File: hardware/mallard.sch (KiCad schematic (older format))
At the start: 84 parts, among them J1 USB_A, J2 Conn_02x03_Odd_Even, J3 Conn_01x03, J4 Conn_01x03, J5 Conn_01x03, J6 Conn_01x03, SW1 RESET Switch, U1 TMP235, U10 LM828, U11 STM32L4Q5xx, U12 LTC3529EDCB, U2 TMP235, U3 TMP235, U4 BQ24210DQCT, U5 TMUX1309, U6 TMUX1309, U7 LMP7721, U8 TPS71710DRVR, U9 LMV554

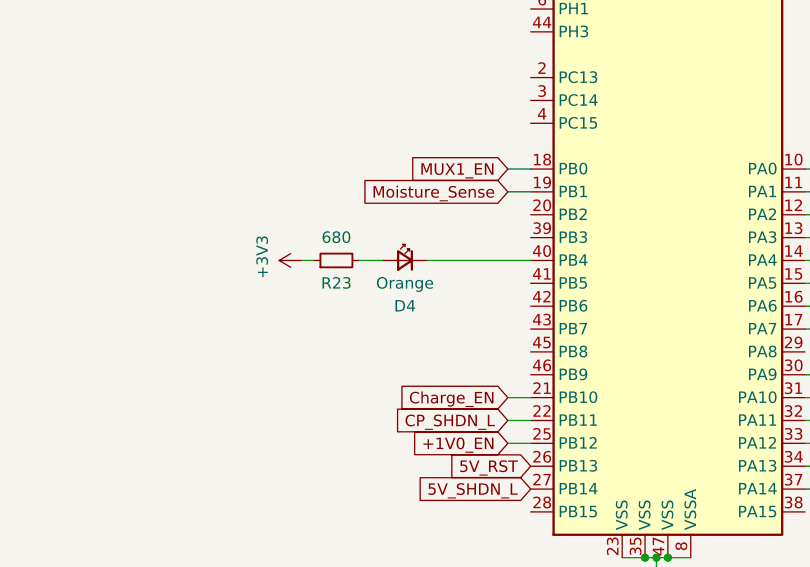
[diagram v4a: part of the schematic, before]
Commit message: Found alts for passives
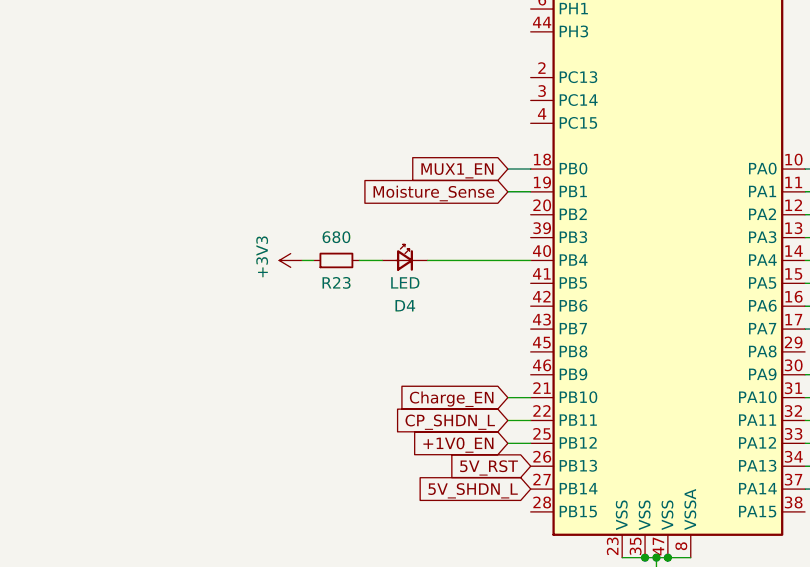
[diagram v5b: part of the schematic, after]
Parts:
- C1, C10, C12, C13, C14, C15, C2, C21, C3, C4, C5, C6, C7, C8, C9: Digikey 311-1446-1-ND -> CL10B105KO8NNNC
- D1: Digikey S1B-FDICT-ND -> S1BFSCT-ND
- D4: value Orange -> LED; footprint Diode_SMD:D_0805_2012Metric_Castellated -> LED_SMD:LED_0603_1608Metric_Pad1.05x0.95mm_HandSolder; Digikey 160-1413-1-ND -> 1497-1215-1-ND
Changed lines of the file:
@@
 AR Path="/61F56C19" Ref="D4"  Part="1"
 F 0 "D4" H 15900 6050 50  0000 C CNN
-F 1 "Orange" H 15900 6150 50  0000 C CNN
-F 2 "Diode_SMD:D_0805_2012Metric_Castellated" V 15900 6250 50  0001 C CNN
-F 3 "https://optoelectronics.liteon.com/upload/download/DS-22-99-0185/LTST-C170KFKT.pdf" V 15900 6250 50  0001 C CNN
-F 4 "160-1413-1-ND" H 15900 6250 50  0001 C CNN "Digikey"
+F 1 "LED" H 15900 6150 50  0000 C CNN
+F 2 "LED_SMD:LED_0603_1608Metric_Pad1.05x0.95mm_HandSolder" V 15900 6250 50  0001 C CNN
+F 3 "https://www.sunledusa.com/products/spec/XZVG53W-8.pdf" V 15900 6250 50  0001 C CNN
+F 4 "1497-1215-1-ND" H 15900 6250 50  0001 C CNN "Digikey"
 	1    15900 6250
 	-1   0    0    -1
@@
 F 1 "1uF" H -3535 12705 50  0000 L CNN
 F 2 "Capacitor_SMD:C_0603_1608Metric_Pad1.08x0.95mm_HandSolder" H -3612 12600 50  0001 C CNN
-F 3 "https://www.yageo.com/upload/media/product/productsearch/datasheet/mlcc/UPY-GPHC_X7R_6.3V-to-50V_20.pdf" H -3650 12750 50  0001 C CNN
-F 4 "311-1446-1-ND" H -3650 12750 50  0001 C CNN "Digikey"
+F 3 "http://weblib.samsungsem.com/mlcc/mlcc-ec-data-sheet.do?partNumber=CL10B105KO8NNN" H -3650 12750 50  0001 C CNN
+F 4 "CL10B105KO8NNNC" H -3650 12750 50  0001 C CNN "Digikey"
 	1    -3650 12750
 	1    0    0    -1
@@
 F 1 "1uF" H -2585 9455 50  0000 L CNN
 F 2 "Capacitor_SMD:C_0603_1608Metric_Pad1.08x0.95mm_HandSolder" H -2662 9350 50  0001 C CNN
-F 3 "https://www.yageo.com/upload/media/product/productsearch/datasheet/mlcc/UPY-GPHC_X7R_6.3V-to-50V_20.pdf" H -2700 9500 50  0001 C CNN
-F 4 "311-1446-1-ND" H -2700 9500 50  0001 C CNN "Digikey"
+F 3 "http://weblib.samsungsem.com/mlcc/mlcc-ec-data-sheet.do?partNumber=CL10B105KO8NNN" H -2700 9500 50  0001 C CNN
+F 4 "CL10B105KO8NNNC" H -2700 9500 50  0001 C CNN "Digikey"
 	1    -2700 9500
 	1    0    0    -1
@@
 F 1 "1uF" H -2385 11855 50  0000 L CNN
 F 2 "Capacitor_SMD:C_0603_1608Metric_Pad1.08x0.95mm_HandSolder" H -2462 11750 50  0001 C CNN
-F 3 "https://www.yageo.com/upload/media/product/productsearch/datasheet/mlcc/UPY-GPHC_X7R_6.3V-to-50V_20.pdf" H -2500 11900 50  0001 C CNN
-F 4 "311-1446-1-ND" H -2500 11900 50  0001 C CNN "Digikey"
+F 3 "http://weblib.samsungsem.com/mlcc/mlcc-ec-data-sheet.do?partNumber=CL10B105KO8NNN" H -2500 11900 50  0001 C CNN
+F 4 "CL10B105KO8NNNC" H -2500 11900 50  0001 C CNN "Digikey"
 	1    -2500 11900
 	1    0    0    -1
@@
 F 1 "1uF" H 2265 10055 50  0000 L CNN
 F 2 "Capacitor_SMD:C_0603_1608Metric_Pad1.08x0.95mm_HandSolder" H 2188 9950 50  0001 C CNN
-F 3 "https://www.yageo.com/upload/media/product/productsearch/datasheet/mlcc/UPY-GPHC_X7R_6.3V-to-50V_20.pdf" H 2150 10100 50  0001 C CNN
-F 4 "311-1446-1-ND" H 2150 10100 50  0001 C CNN "Digikey"
+F 3 "http://weblib.samsungsem.com/mlcc/mlcc-ec-data-sheet.do?partNumber=CL10B105KO8NNN" H 2150 10100 50  0001 C CNN
+F 4 "CL10B105KO8NNNC" H 2150 10100 50  0001 C CNN "Digikey"
 	1    2150 10100
 	1    0    0    -1
@@
 F 1 "1uF" H 1815 11055 50  0000 L CNN
 F 2 "Capacitor_SMD:C_0603_1608Metric_Pad1.08x0.95mm_HandSolder" H 1738 10950 50  0001 C CNN
-F 3 "https://www.yageo.com/upload/media/product/productsearch/datasheet/mlcc/UPY-GPHC_X7R_6.3V-to-50V_20.pdf" H 1700 11100 50  0001 C CNN
-F 4 "311-1446-1-ND" H 1700 11100 50  0001 C CNN "Digikey"
+F 3 "http://weblib.samsungsem.com/mlcc/mlcc-ec-data-sheet.do?partNumber=CL10B105KO8NNN" H 1700 11100 50  0001 C CNN
+F 4 "CL10B105KO8NNNC" H 1700 11100 50  0001 C CNN "Digikey"
 	1    1700 11100
 	1    0    0    -1
@@
 F 1 "1uF" H 6315 3255 50  0000 L CNN
 F 2 "Capacitor_SMD:C_0603_1608Metric_Pad1.08x0.95mm_HandSolder" H 6238 3150 50  0001 C CNN
-F 3 "https://www.yageo.com/upload/media/product/productsearch/datasheet/mlcc/UPY-GPHC_X7R_6.3V-to-50V_20.pdf" H 6200 3300 50  0001 C CNN
-F 4 "311-1446-1-ND" H 6200 3300 50  0001 C CNN "Digikey"
+F 3 "http://weblib.samsungsem.com/mlcc/mlcc-ec-data-sheet.do?partNumber=CL10B105KO8NNN" H 6200 3300 50  0001 C CNN
+F 4 "CL10B105KO8NNNC" H 6200 3300 50  0001 C CNN "Digikey"
 	1    6200 3300
 	1    0    0    -1
@@
 F 2 "Diode_SMD:D_SMA_Handsoldering" H 1600 3000 50  0001 C CNN
 F 3 "https://www.diodes.com/assets/Datasheets/ds16003.pdf" H 1600 3000 50  0001 C CNN
-F 4 "S1B-FDICT-ND" H 1600 3000 50  0001 C CNN "Digikey"
+F 4 "S1BFSCT-ND" H 1600 3000 50  0001 C CNN "Digikey"
 	1    1600 3000
 	-1   0    0    1
@@
 F 1 "1uF" H 8065 4605 50  0000 L CNN
 F 2 "Capacitor_SMD:C_0603_1608Metric_Pad1.08x0.95mm_HandSolder" H 7988 4500 50  0001 C CNN
-F 3 "https://www.yageo.com/upload/media/product/productsearch/datasheet/mlcc/UPY-GPHC_X7R_6.3V-to-50V_20.pdf" H 7950 4650 50  0001 C CNN
-F 4 "311-1446-1-ND" H 7950 4650 50  0001 C CNN "Digikey"
+F 3 "http://weblib.samsungsem.com/mlcc/mlcc-ec-data-sheet.do?partNumber=CL10B105KO8NNN" H 7950 4650 50  0001 C CNN
+F 4 "CL10B105KO8NNNC" H 7950 4650 50  0001 C CNN "Digikey"
 	1    7950 4650
 	1    0    0    -1
@@
 F 1 "1uF" H 10265 4605 50  0000 L CNN
 F 2 "Capacitor_SMD:C_0603_1608Metric_Pad1.08x0.95mm_HandSolder" H 10188 4500 50  0001 C CNN
-F 3 "https://www.yageo.com/upload/media/product/productsearch/datasheet/mlcc/UPY-GPHC_X7R_6.3V-to-50V_20.pdf" H 10150 4650 50  0001 C CNN
-F 4 "311-1446-1-ND" H 10150 4650 50  0001 C CNN "Digikey"
+F 3 "http://weblib.samsungsem.com/mlcc/mlcc-ec-data-sheet.do?partNumber=CL10B105KO8NNN" H 10150 4650 50  0001 C CNN
+F 4 "CL10B105KO8NNNC" H 10150 4650 50  0001 C CNN "Digikey"
 	1    10150 4650
 	1    0    0    -1
@@
 F 1 "1uF" H 2265 3205 50  0000 L CNN
 F 2 "Capacitor_SMD:C_0603_1608Metric_Pad1.08x0.95mm_HandSolder" H 2188 3100 50  0001 C CNN
-F 3 "https://www.yageo.com/upload/media/product/productsearch/datasheet/mlcc/UPY-GPHC_X7R_6.3V-to-50V_20.pdf" H 2150 3250 50  0001 C CNN
-F 4 "311-1446-1-ND" H 2150 3250 50  0001 C CNN "Digikey"
+F 3 "http://weblib.samsungsem.com/mlcc/mlcc-ec-data-sheet.do?partNumber=CL10B105KO8NNN" H 2150 3250 50  0001 C CNN
+F 4 "CL10B105KO8NNNC" H 2150 3250 50  0001 C CNN "Digikey"
 	1    2150 3250
 	1    0    0    -1
@@
 F 1 "1uF" H -585 9255 50  0000 L CNN
 F 2 "Capacitor_SMD:C_0603_1608Metric_Pad1.08x0.95mm_HandSolder" H -662 9150 50  0001 C CNN
-F 3 "https://www.yageo.com/upload/media/product/productsearch/datasheet/mlcc/UPY-GPHC_X7R_6.3V-to-50V_20.pdf" H -700 9300 50  0001 C CNN
-F 4 "311-1446-1-ND" H -700 9300 50  0001 C CNN "Digikey"
+F 3 "http://weblib.samsungsem.com/mlcc/mlcc-ec-data-sheet.do?partNumber=CL10B105KO8NNN" H -700 9300 50  0001 C CNN
+F 4 "CL10B105KO8NNNC" H -700 9300 50  0001 C CNN "Digikey"
 	1    -700 9300
 	1    0    0    -1
@@
 F 1 "1uF" H -3285 14705 50  0000 L CNN
 F 2 "Capacitor_SMD:C_0603_1608Metric_Pad1.08x0.95mm_HandSolder" H -3362 14600 50  0001 C CNN
-F 3 "https://www.yageo.com/upload/media/product/productsearch/datasheet/mlcc/UPY-GPHC_X7R_6.3V-to-50V_20.pdf" H -3400 14750 50  0001 C CNN
-F 4 "311-1446-1-ND" H -3400 14750 50  0001 C CNN "Digikey"
+F 3 "http://weblib.samsungsem.com/mlcc/mlcc-ec-data-sheet.do?partNumber=CL10B105KO8NNN" H -3400 14750 50  0001 C CNN
+F 4 "CL10B105KO8NNNC" H -3400 14750 50  0001 C CNN "Digikey"
 	1    -3400 14750
 	1    0    0    -1
@@
 F 1 "1uF" H -3285 13705 50  0000 L CNN
 F 2 "Capacitor_SMD:C_0603_1608Metric_Pad1.08x0.95mm_HandSolder" H -3362 13600 50  0001 C CNN
-F 3 "https://www.yageo.com/upload/media/product/productsearch/datasheet/mlcc/UPY-GPHC_X7R_6.3V-to-50V_20.pdf" H -3400 13750 50  0001 C CNN
-F 4 "311-1446-1-ND" H -3400 13750 50  0001 C CNN "Digikey"
+F 3 "http://weblib.samsungsem.com/mlcc/mlcc-ec-data-sheet.do?partNumber=CL10B105KO8NNN" H -3400 13750 50  0001 C CNN
+F 4 "CL10B105KO8NNNC" H -3400 13750 50  0001 C CNN "Digikey"
 	1    -3400 13750
 	1    0    0    -1
@@
 F 1 "1uF" H -385 8505 50  0000 L CNN
 F 2 "Capacitor_SMD:C_0603_1608Metric_Pad1.08x0.95mm_HandSolder" H -462 8400 50  0001 C CNN
-F 3 "https://www.yageo.com/upload/media/product/productsearch/datasheet/mlcc/UPY-GPHC_X7R_6.3V-to-50V_20.pdf" H -500 8550 50  0001 C CNN
-F 4 "311-1446-1-ND" H -500 8550 50  0001 C CNN "Digikey"
+F 3 "http://weblib.samsungsem.com/mlcc/mlcc-ec-data-sheet.do?partNumber=CL10B105KO8NNN" H -500 8550 50  0001 C CNN
+F 4 "CL10B105KO8NNNC" H -500 8550 50  0001 C CNN "Digikey"
 	1    -500 8550
 	1    0    0    -1
@@
 F 1 "1uF" H 8215 3205 50  0000 L CNN
 F 2 "Capacitor_SMD:C_0603_1608Metric_Pad1.08x0.95mm_HandSolder" H 8138 3100 50  0001 C CNN
-F 3 "https://www.yageo.com/upload/media/product/productsearch/datasheet/mlcc/UPY-GPHC_X7R_6.3V-to-50V_20.pdf" H 8100 3250 50  0001 C CNN
-F 4 "311-1446-1-ND" H 8100 3250 50  0001 C CNN "Digikey"
+F 3 "http://weblib.samsungsem.com/mlcc/mlcc-ec-data-sheet.do?partNumber=CL10B105KO8NNN" H 8100 3250 50  0001 C CNN
+F 4 "CL10B105KO8NNNC" H 8100 3250 50  0001 C CNN "Digikey"
 	1    8100 3250
 	1    0    0    -1
@@
 F 1 "1uF" H 10465 3205 50  0000 L CNN
 F 2 "Capacitor_SMD:C_0603_1608Metric_Pad1.08x0.95mm_HandSolder" H 10388 3100 50  0001 C CNN
-F 3 "https://www.yageo.com/upload/media/product/productsearch/datasheet/mlcc/UPY-GPHC_X7R_6.3V-to-50V_20.pdf" H 10350 3250 50  0001 C CNN
-F 4 "311-1446-1-ND" H 10350 3250 50  0001 C CNN "Digikey"
+F 3 "http://weblib.samsungsem.com/mlcc/mlcc-ec-data-sheet.do?partNumber=CL10B105KO8NNN" H 10350 3250 50  0001 C CNN
+F 4 "CL10B105KO8NNNC" H 10350 3250 50  0001 C CNN "Digikey"
 	1    10350 3250
 	1    0    0    -1

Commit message: Updated digikey part #
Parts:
- C1, C10, C12, C13, C14, C15, C2, C21, C3, C4, C5, C6, C7, C8, C9: Digikey CL10B105KO8NNNC -> 1276-1019-1-ND
- R13, R17, R4, R6, R8: Digikey 13-RC0603DR-0710KLCT-ND -> 13-AC0603DR-0710KLCT-ND
- R14: Digikey 541-2788-1-ND -> RHM1.00KADCT-ND
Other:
- note removed: "Check Symbol with Datasheet to make sure pins match"
- note removed: "Double check footprint for USB connector"
- note removed: "Wrong footprint size"
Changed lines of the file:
@@
 Wire Wire Line
 	16450 4850 16300 4850
-Text Notes 17750 5400 0    50   ~ 0
-Check Symbol with Datasheet to make sure pins match
 Wire Wire Line
 	17000 7550 17000 7650
@@
 	1    0    0    -1
 $EndComp
-Text Notes 15050 2350 0    50   ~ 0
-Double check footprint for USB connector
 Wire Wire Line
 	17450 2400 17450 2550
@@
 F 2 "Resistor_SMD:R_0603_1608Metric_Pad0.98x0.95mm_HandSolder" V -720 10550 50  0001 C CNN
 F 3 "https://www.yageo.com/upload/media/product/productsearch/datasheet/rchip/PYu-RC_Group_51_RoHS_L_11.pdf" H -650 10550 50  0001 C CNN
-F 4 "13-RC0603DR-0710KLCT-ND" V -650 10550 50  0001 C CNN "Digikey"
+F 4 "13-AC0603DR-0710KLCT-ND" V -650 10550 50  0001 C CNN "Digikey"
 	1    -650 10550
 	0    1    1    0
@@
 F 2 "Resistor_SMD:R_0603_1608Metric_Pad0.98x0.95mm_HandSolder" V 2980 12800 50  0001 C CNN
 F 3 "https://www.vishay.com/docs/20065/rcse3.pdf" H 3050 12800 50  0001 C CNN
-F 4 "541-2788-1-ND" H 3050 12800 50  0001 C CNN "Digikey"
+F 4 "RHM1.00KADCT-ND" H 3050 12800 50  0001 C CNN "Digikey"
 	1    3050 12800
 	1    0    0    -1
@@
 F 2 "Resistor_SMD:R_0603_1608Metric_Pad0.98x0.95mm_HandSolder" V -70 10300 50  0001 C CNN
 F 3 "https://www.yageo.com/upload/media/product/productsearch/datasheet/rchip/PYu-RC_Group_51_RoHS_L_11.pdf" H 0   10300 50  0001 C CNN
-F 4 "13-RC0603DR-0710KLCT-ND" V 0   10300 50  0001 C CNN "Digikey"
+F 4 "13-AC0603DR-0710KLCT-ND" V 0   10300 50  0001 C CNN "Digikey"
 	1    0    10300
 	-1   0    0    1
@@
 F 2 "Resistor_SMD:R_0603_1608Metric_Pad0.98x0.95mm_HandSolder" V 3380 9850 50  0001 C CNN
 F 3 "https://www.yageo.com/upload/media/product/productsearch/datasheet/rchip/PYu-RC_Group_51_RoHS_L_11.pdf" H 3450 9850 50  0001 C CNN
-F 4 "13-RC0603DR-0710KLCT-ND" V 3450 9850 50  0001 C CNN "Digikey"
+F 4 "13-AC0603DR-0710KLCT-ND" V 3450 9850 50  0001 C CNN "Digikey"
 	1    3450 9850
 	0    1    1    0
@@
 F 2 "Resistor_SMD:R_0603_1608Metric_Pad0.98x0.95mm_HandSolder" V 2730 13600 50  0001 C CNN
 F 3 "https://www.yageo.com/upload/media/product/productsearch/datasheet/rchip/PYu-RC_Group_51_RoHS_L_11.pdf" H 2800 13600 50  0001 C CNN
-F 4 "13-RC0603DR-0710KLCT-ND" V 2800 13600 50  0001 C CNN "Digikey"
+F 4 "13-AC0603DR-0710KLCT-ND" V 2800 13600 50  0001 C CNN "Digikey"
 	1    2800 13600
 	-1   0    0    1
@@
 F 2 "Capacitor_SMD:C_0603_1608Metric_Pad1.08x0.95mm_HandSolder" H -3612 12600 50  0001 C CNN
 F 3 "http://weblib.samsungsem.com/mlcc/mlcc-ec-data-sheet.do?partNumber=CL10B105KO8NNN" H -3650 12750 50  0001 C CNN
-F 4 "CL10B105KO8NNNC" H -3650 12750 50  0001 C CNN "Digikey"
+F 4 "1276-1019-1-ND" H -3650 12750 50  0001 C CNN "Digikey"
 	1    -3650 12750
 	1    0    0    -1
@@
 F 2 "Capacitor_SMD:C_0603_1608Metric_Pad1.08x0.95mm_HandSolder" H -2662 9350 50  0001 C CNN
 F 3 "http://weblib.samsungsem.com/mlcc/mlcc-ec-data-sheet.do?partNumber=CL10B105KO8NNN" H -2700 9500 50  0001 C CNN
-F 4 "CL10B105KO8NNNC" H -2700 9500 50  0001 C CNN "Digikey"
+F 4 "1276-1019-1-ND" H -2700 9500 50  0001 C CNN "Digikey"
 	1    -2700 9500
 	1    0    0    -1
@@
 F 2 "Capacitor_SMD:C_0603_1608Metric_Pad1.08x0.95mm_HandSolder" H -2462 11750 50  0001 C CNN
 F 3 "http://weblib.samsungsem.com/mlcc/mlcc-ec-data-sheet.do?partNumber=CL10B105KO8NNN" H -2500 11900 50  0001 C CNN
-F 4 "CL10B105KO8NNNC" H -2500 11900 50  0001 C CNN "Digikey"
+F 4 "1276-1019-1-ND" H -2500 11900 50  0001 C CNN "Digikey"
 	1    -2500 11900
 	1    0    0    -1
@@
 F 2 "Capacitor_SMD:C_0603_1608Metric_Pad1.08x0.95mm_HandSolder" H 2188 9950 50  0001 C CNN
 F 3 "http://weblib.samsungsem.com/mlcc/mlcc-ec-data-sheet.do?partNumber=CL10B105KO8NNN" H 2150 10100 50  0001 C CNN
-F 4 "CL10B105KO8NNNC" H 2150 10100 50  0001 C CNN "Digikey"
+F 4 "1276-1019-1-ND" H 2150 10100 50  0001 C CNN "Digikey"
 	1    2150 10100
 	1    0    0    -1
@@
 F 2 "Capacitor_SMD:C_0603_1608Metric_Pad1.08x0.95mm_HandSolder" H 1738 10950 50  0001 C CNN
 F 3 "http://weblib.samsungsem.com/mlcc/mlcc-ec-data-sheet.do?partNumber=CL10B105KO8NNN" H 1700 11100 50  0001 C CNN
-F 4 "CL10B105KO8NNNC" H 1700 11100 50  0001 C CNN "Digikey"
+F 4 "1276-1019-1-ND" H 1700 11100 50  0001 C CNN "Digikey"
 	1    1700 11100
 	1    0    0    -1
@@
 F 2 "Capacitor_SMD:C_0603_1608Metric_Pad1.08x0.95mm_HandSolder" H 6238 3150 50  0001 C CNN
 F 3 "http://weblib.samsungsem.com/mlcc/mlcc-ec-data-sheet.do?partNumber=CL10B105KO8NNN" H 6200 3300 50  0001 C CNN
-F 4 "CL10B105KO8NNNC" H 6200 3300 50  0001 C CNN "Digikey"
+F 4 "1276-1019-1-ND" H 6200 3300 50  0001 C CNN "Digikey"
 	1    6200 3300
 	1    0    0    -1
@@
 F 2 "Capacitor_SMD:C_0603_1608Metric_Pad1.08x0.95mm_HandSolder" H 7988 4500 50  0001 C CNN
 F 3 "http://weblib.samsungsem.com/mlcc/mlcc-ec-data-sheet.do?partNumber=CL10B105KO8NNN" H 7950 4650 50  0001 C CNN
-F 4 "CL10B105KO8NNNC" H 7950 4650 50  0001 C CNN "Digikey"
+F 4 "1276-1019-1-ND" H 7950 4650 50  0001 C CNN "Digikey"
 	1    7950 4650
 	1    0    0    -1
@@
 F 2 "Capacitor_SMD:C_0603_1608Metric_Pad1.08x0.95mm_HandSolder" H 10188 4500 50  0001 C CNN
 F 3 "http://weblib.samsungsem.com/mlcc/mlcc-ec-data-sheet.do?partNumber=CL10B105KO8NNN" H 10150 4650 50  0001 C CNN
-F 4 "CL10B105KO8NNNC" H 10150 4650 50  0001 C CNN "Digikey"
+F 4 "1276-1019-1-ND" H 10150 4650 50  0001 C CNN "Digikey"
 	1    10150 4650
 	1    0    0    -1
@@
 F 2 "Capacitor_SMD:C_0603_1608Metric_Pad1.08x0.95mm_HandSolder" H 2188 3100 50  0001 C CNN
 F 3 "http://weblib.samsungsem.com/mlcc/mlcc-ec-data-sheet.do?partNumber=CL10B105KO8NNN" H 2150 3250 50  0001 C CNN
-F 4 "CL10B105KO8NNNC" H 2150 3250 50  0001 C CNN "Digikey"
+F 4 "1276-1019-1-ND" H 2150 3250 50  0001 C CNN "Digikey"
 	1    2150 3250
 	1    0    0    -1
@@
 F 2 "Capacitor_SMD:C_0603_1608Metric_Pad1.08x0.95mm_HandSolder" H -662 9150 50  0001 C CNN
 F 3 "http://weblib.samsungsem.com/mlcc/mlcc-ec-data-sheet.do?partNumber=CL10B105KO8NNN" H -700 9300 50  0001 C CNN
-F 4 "CL10B105KO8NNNC" H -700 9300 50  0001 C CNN "Digikey"
+F 4 "1276-1019-1-ND" H -700 9300 50  0001 C CNN "Digikey"
 	1    -700 9300
 	1    0    0    -1
@@
 F 2 "Capacitor_SMD:C_0603_1608Metric_Pad1.08x0.95mm_HandSolder" H -3362 14600 50  0001 C CNN
 F 3 "http://weblib.samsungsem.com/mlcc/mlcc-ec-data-sheet.do?partNumber=CL10B105KO8NNN" H -3400 14750 50  0001 C CNN
-F 4 "CL10B105KO8NNNC" H -3400 14750 50  0001 C CNN "Digikey"
+F 4 "1276-1019-1-ND" H -3400 14750 50  0001 C CNN "Digikey"
 	1    -3400 14750
 	1    0    0    -1
@@
 F 2 "Capacitor_SMD:C_0603_1608Metric_Pad1.08x0.95mm_HandSolder" H -3362 13600 50  0001 C CNN
 F 3 "http://weblib.samsungsem.com/mlcc/mlcc-ec-data-sheet.do?partNumber=CL10B105KO8NNN" H -3400 13750 50  0001 C CNN
-F 4 "CL10B105KO8NNNC" H -3400 13750 50  0001 C CNN "Digikey"
+F 4 "1276-1019-1-ND" H -3400 13750 50  0001 C CNN "Digikey"
 	1    -3400 13750
 	1    0    0    -1
@@
 Wire Wire Line
 	-3400 13600 -3500 13600
-Text Notes -900 10700 0    50   ~ 0
-Wrong footprint size
-Text Notes 1700 8450 0    50   ~ 0
-Wrong footprint size
-Text Notes 3850 9300 0    50   ~ 0
-Wrong footprint size
-Text Notes 3400 12800 0    50   ~ 0
-Wrong footprint size
 $Comp
 L mallard-rescue:LTC3529EDCB-mallard U12
@@
 F 2 "Capacitor_SMD:C_0603_1608Metric_Pad1.08x0.95mm_HandSolder" H -462 8400 50  0001 C CNN
 F 3 "http://weblib.samsungsem.com/mlcc/mlcc-ec-data-sheet.do?partNumber=CL10B105KO8NNN" H -500 8550 50  0001 C CNN
-F 4 "CL10B105KO8NNNC" H -500 8550 50  0001 C CNN "Digikey"
+F 4 "1276-1019-1-ND" H -500 8550 50  0001 C CNN "Digikey"
 	1    -500 8550
 	1    0    0    -1
@@
 F 2 "Resistor_SMD:R_0603_1608Metric_Pad0.98x0.95mm_HandSolder" V 1380 8550 50  0001 C CNN
 F 3 "https://www.yageo.com/upload/media/product/productsearch/datasheet/rchip/PYu-RC_Group_51_RoHS_L_11.pdf" H 1450 8550 50  0001 C CNN
-F 4 "13-RC0603DR-0710KLCT-ND" V 1450 8550 50  0001 C CNN "Digikey"
+F 4 "13-AC0603DR-0710KLCT-ND" V 1450 8550 50  0001 C CNN "Digikey"
 	1    1450 8550
 	0    1    1    0
@@
 F 2 "Capacitor_SMD:C_0603_1608Metric_Pad1.08x0.95mm_HandSolder" H 8138 3100 50  0001 C CNN
 F 3 "http://weblib.samsungsem.com/mlcc/mlcc-ec-data-sheet.do?partNumber=CL10B105KO8NNN" H 8100 3250 50  0001 C CNN
-F 4 "CL10B105KO8NNNC" H 8100 3250 50  0001 C CNN "Digikey"
+F 4 "1276-1019-1-ND" H 8100 3250 50  0001 C CNN "Digikey"
 	1    8100 3250
 	1    0    0    -1
@@
 F 2 "Capacitor_SMD:C_0603_1608Metric_Pad1.08x0.95mm_HandSolder" H 10388 3100 50  0001 C CNN
 F 3 "http://weblib.samsungsem.com/mlcc/mlcc-ec-data-sheet.do?partNumber=CL10B105KO8NNN" H 10350 3250 50  0001 C CNN
-F 4 "CL10B105KO8NNNC" H 10350 3250 50  0001 C CNN "Digikey"
+F 4 "1276-1019-1-ND" H 10350 3250 50  0001 C CNN "Digikey"
 	1    10350 3250
 	1    0    0    -1

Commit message: Tidied up schematic
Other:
- note added: "Microcontroller"
- note added: "Power Input"
- note added: "Sensor Instrumentation"
- note removed: "FOOTPRINT FOR TMP235 IS 5 HOLE CONNECTOR"
- note removed: "I have these switches on hand"
- note removed: "Programming connector copied from a previous project (Flamingo)"
- moved on the sheet: BatteryPack1, C1, C10, C11, C12, C13, C14, C15, C16, C17, C18, C19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
